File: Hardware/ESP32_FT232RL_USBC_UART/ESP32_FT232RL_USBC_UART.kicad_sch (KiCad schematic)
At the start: 25 parts, among them J1 USB_C_Receptacle_USB2.0_16P, J2 Conn_01x04, J3 Conn_01x04, Q1 NPN, Q2 NPN, U2 USBLC6-2SC6, U5 74LVC1G126, U6 74LVC1G126

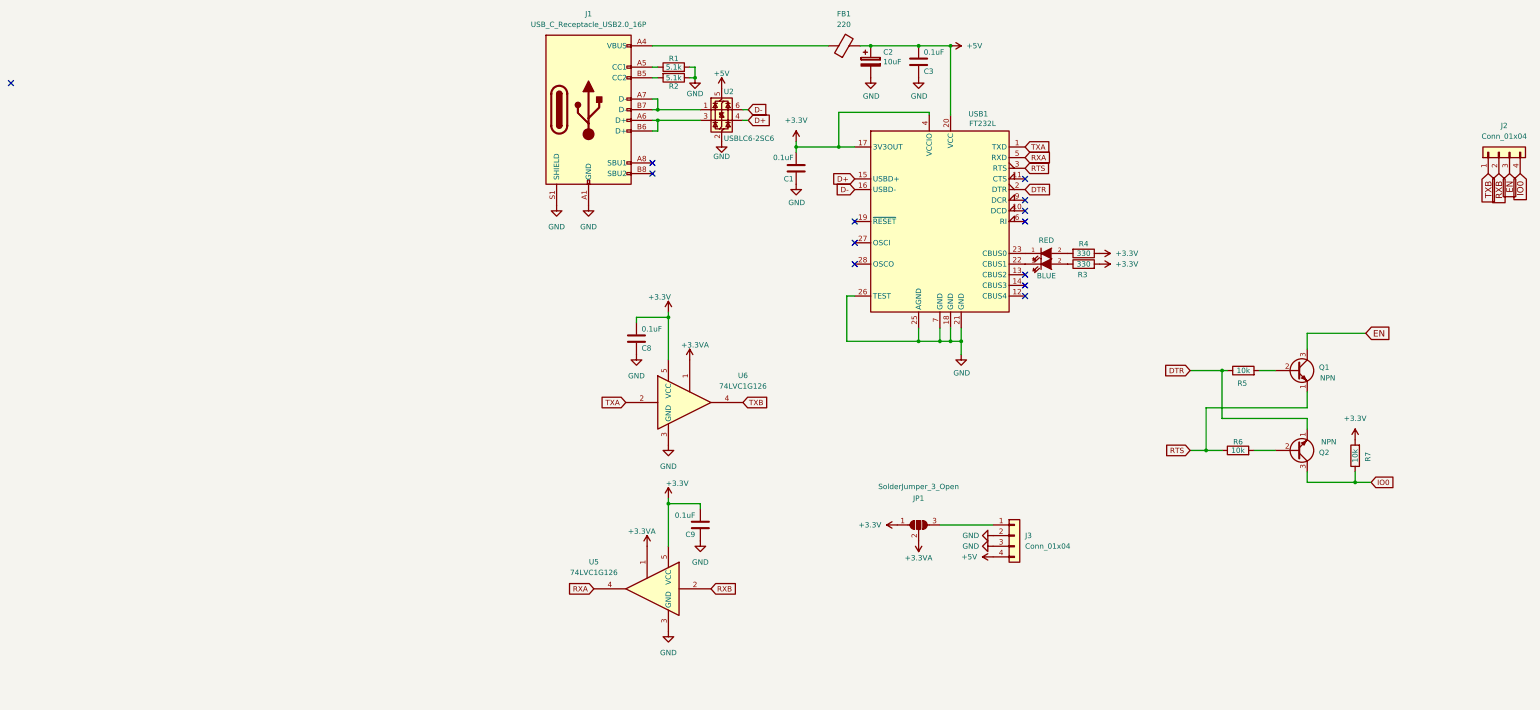
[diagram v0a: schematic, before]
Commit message: Hardware updates. Add Lr04 lora module datasheets
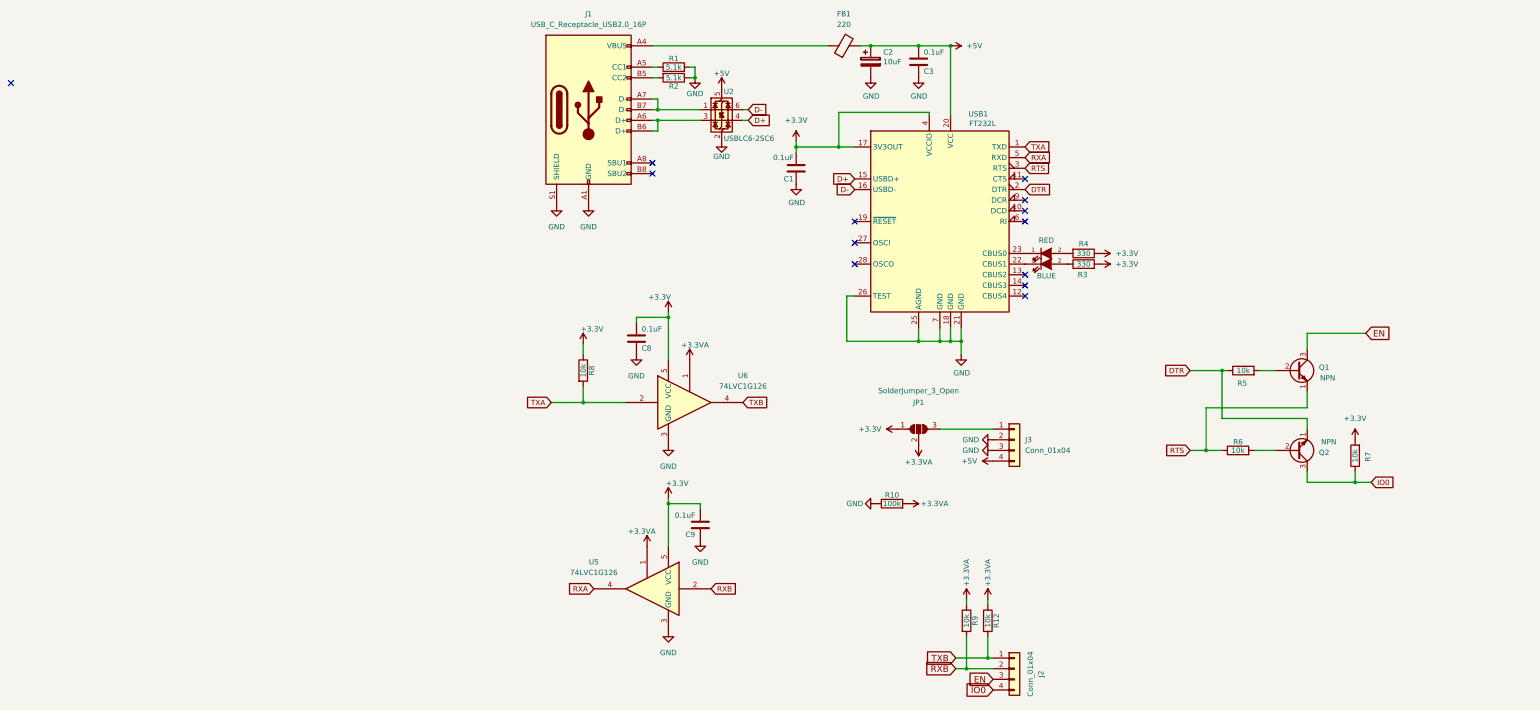
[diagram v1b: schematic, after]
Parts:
- added R10: 100k, Resistor_SMD:R_0805_2012Metric_Pad1.20x1.40mm_HandSolder, symbol Device:R
- added R12, R8, R9: 10k, Resistor_SMD:R_0805_2012Metric_Pad1.20x1.40mm_HandSolder, symbol Device:R
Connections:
- net +3.3V: now also R8.1
- net +3.3VA: now also R10.2, R12.1, R9.1
- net GND: now also R10.1
- net RXB: now also R9.2
- net TXA: now also R8.2
- net TXB: now also R12.2
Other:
- moved on the sheet: J2, J3, JP1
